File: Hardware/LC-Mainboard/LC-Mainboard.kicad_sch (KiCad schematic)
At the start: 1 part

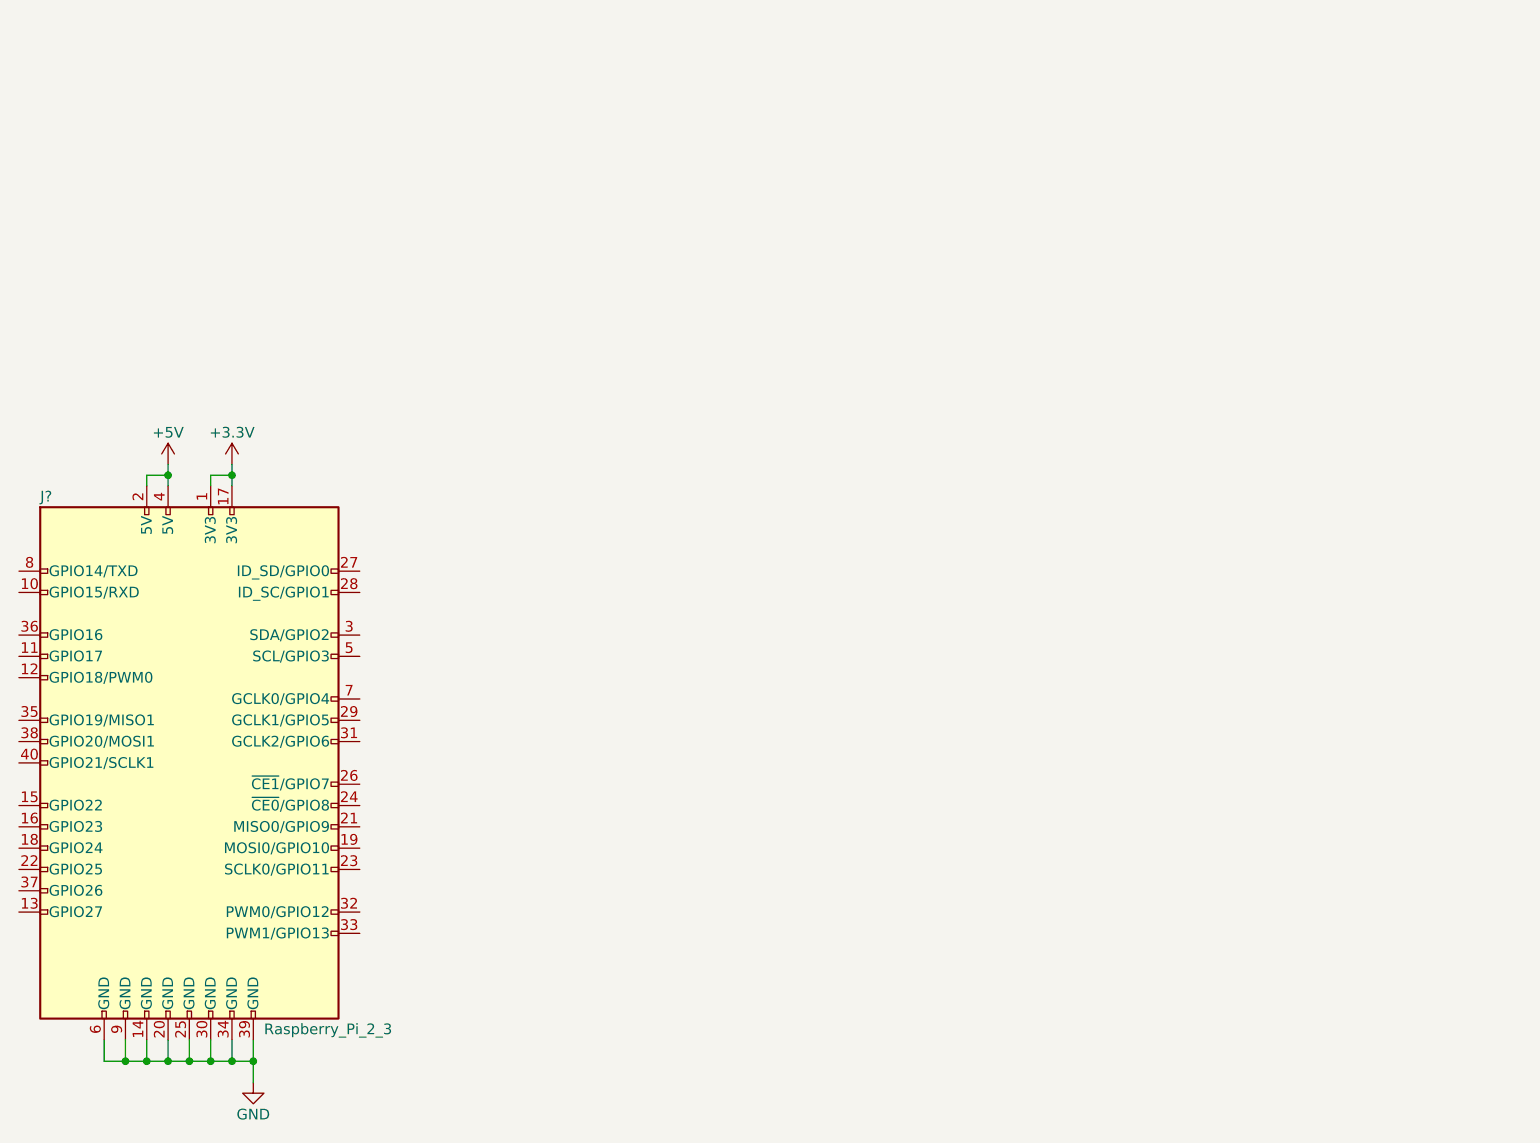
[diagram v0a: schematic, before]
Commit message: Add lib depend, remove bak and boilerplate
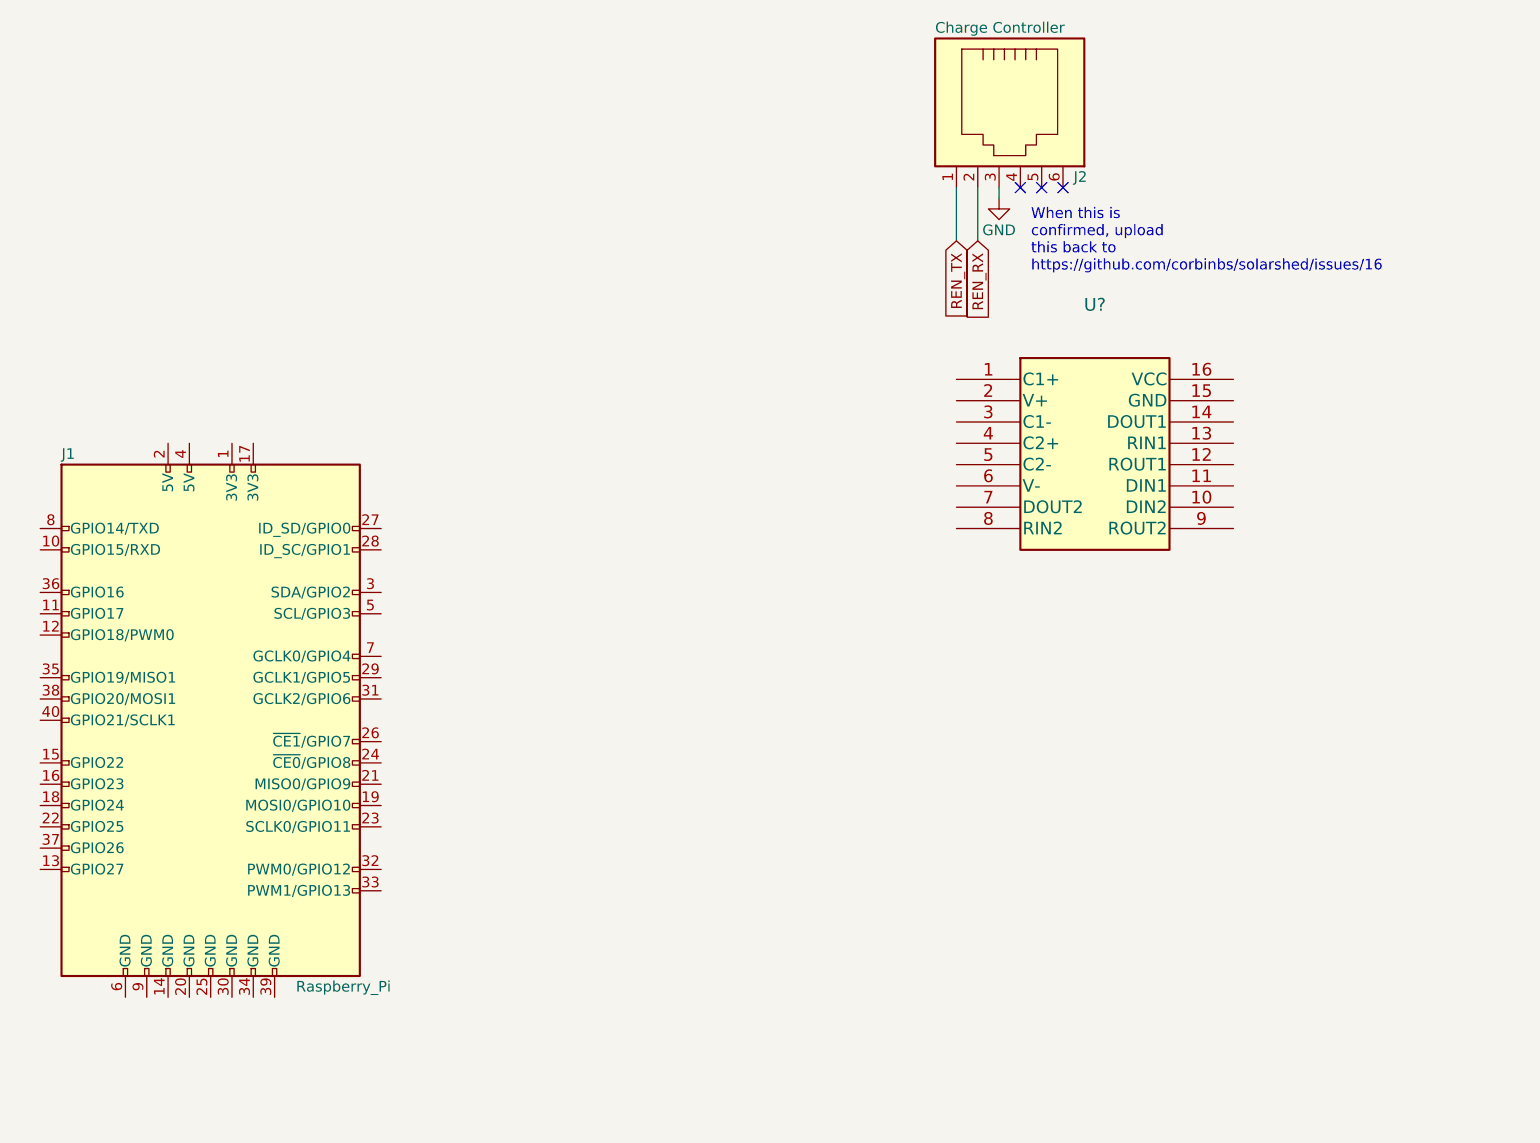
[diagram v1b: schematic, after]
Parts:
- removed J?: Raspberry_Pi_2_3, symbol Connector:Raspberry_Pi_2_3
- added J1: Raspberry_Pi, Connector_PinSocket_2.54mm:PinSocket_2x20_P2.54mm_Vertical, symbol Connector:Raspberry_Pi_2_3
- added J2: Charge Controller, Connector_RJ:RJ12_Amphenol_54601, symbol Connector:RJ12
- added U?: (no value), symbol KenwoodFox:MAX3232IDW
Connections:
- net GND: now also J2.3
- new net REN_RX: J2.2
- new net REN_TX: J2.1
- no-connect marks 0 -> 3
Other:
- note added: "When this is confirmed, upload this back to https://github.com/corbinbs/solarshed/issues/16"

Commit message: Update all
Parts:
- U?: value (none) -> MAX3232IDW; footprint (none) -> KenwoodFox:MAX3232IDW
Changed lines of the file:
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@@
       (effects (font (size 1.524 1.524)))
     )
-    (property "Value" "" (id 1) (at 251.46 52.07 0)
+    (property "Value" "MAX3232IDW" (id 1) (at 251.46 52.07 0)
       (effects (font (size 1.524 1.524)))
     )
-    (property "Footprint" "" (id 2) (at 251.46 66.04 0)
+    (property "Footprint" "KenwoodFox:MAX3232IDW" (id 2) (at 251.46 66.04 0)
       (effects (font (size 1.524 1.524)) hide)
     )

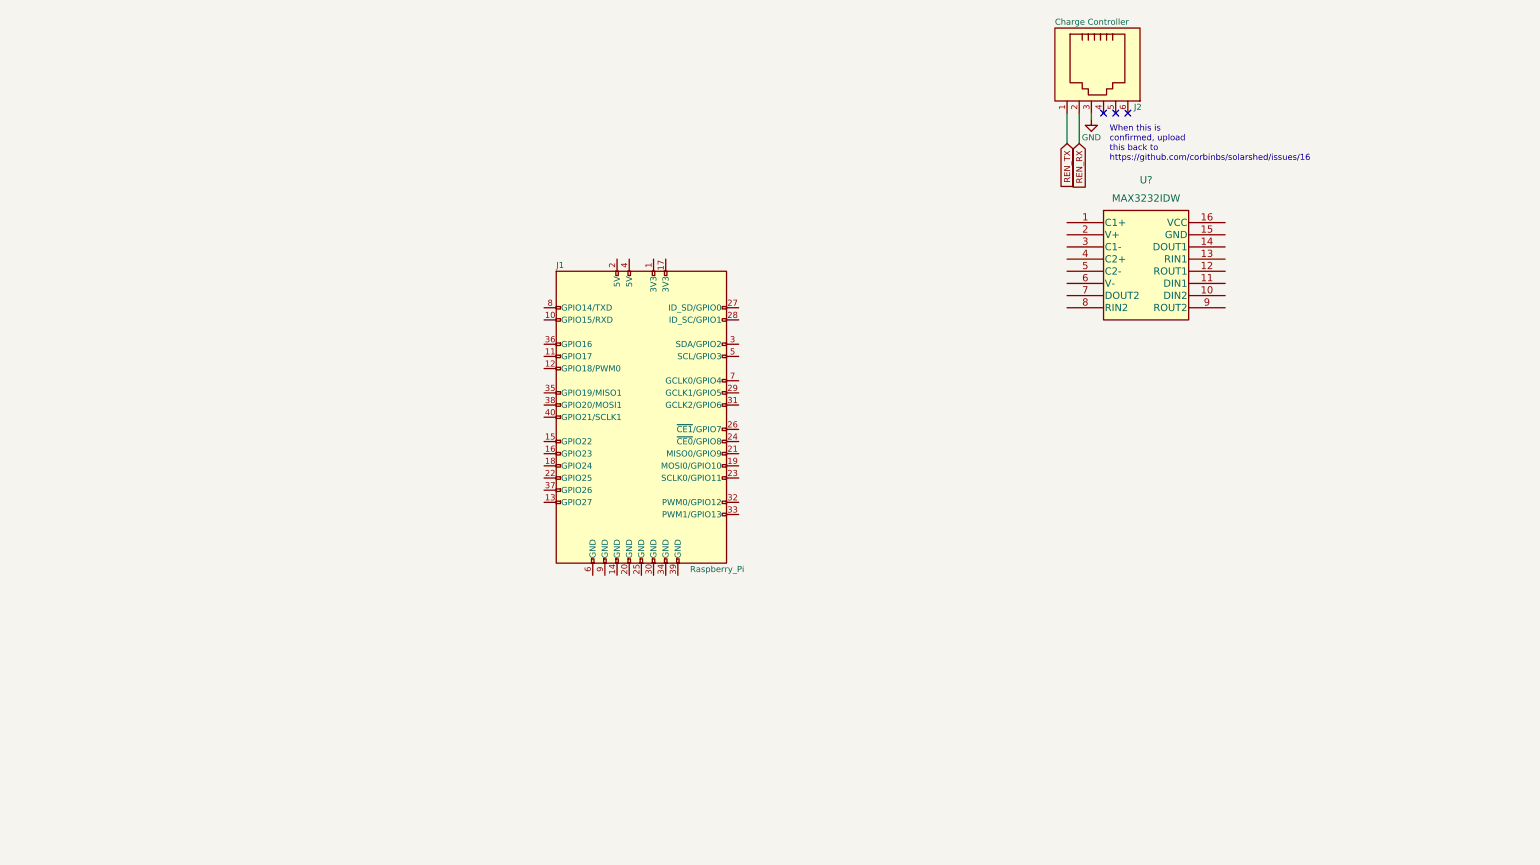
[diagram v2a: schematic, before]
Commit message: Fix encoder spacer, bump lib and implement max3232 in sch
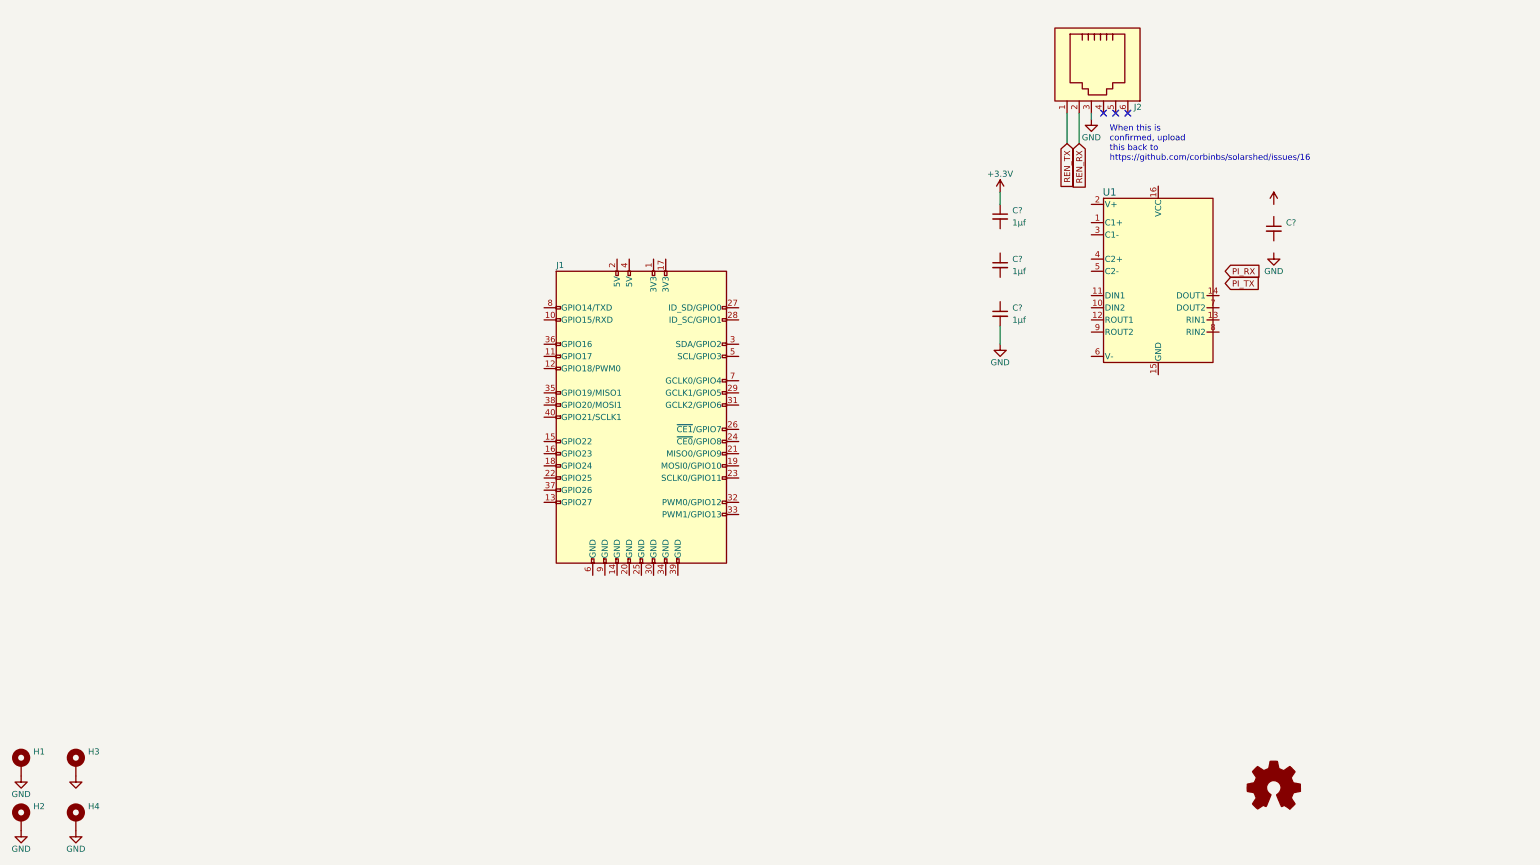
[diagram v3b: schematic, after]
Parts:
- added C? (x3): 1μf, symbol Device:C_Small
- added C?: (no value), symbol Device:C_Small
- added H1, H2, H3, H4: (no value), symbol Mechanical:MountingHole_Pad
- J1: value Raspberry_Pi -> (none); footprint Connector_PinSocket_2.54mm:PinSocket_2x20_P2.54mm_Vertical -> (none)
- J2: value Charge Controller -> (none); footprint Connector_RJ:RJ12_Amphenol_54601 -> (none)
- U1: renamed from U?; value MAX3232IDW -> (none)
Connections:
- net GND: now also C?.2, H1.1, H2.1, H3.1, H4.1
- new net +3V3: C?.1
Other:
- moved on the sheet: U1

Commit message: Bump
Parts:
- removed C? (x2): 1μf, symbol Device:C_Small
- removed C?: (no value), symbol Device:C_Small
- added C1, C3, C4: (no value), symbol Device:C_Small
- added D1, D2: (no value), symbol Device:LED
- added R1, R2: (no value), symbol Device:R_Small
- C2: renamed from C?; value 1μf -> (none)
- U1: footprint KenwoodFox:MAX3232IDW -> (none)
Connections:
- net +3V3: now also J1.1 (3V3), J1.17 (3V3), U1.16 (VCC), C1.1, R1.1, R2.1
- net GND: now also J1.14 (GND), J1.20 (GND), J1.25 (GND), J1.30 (GND), J1.34 (GND), J1.39 (GND), J1.6 (GND), J1.9 (GND), U1.15 (GND), C4.2
- net PI_RX: now also J1.10 (GPIO15/RXD), U1.12 (ROUT1), D1.1 (K)
- net PI_TX: now also J1.8 (GPIO14/TXD), U1.11 (DIN1), D2.1 (K)
- net REN_RX: now also U1.14 (DOUT1)
- net REN_TX: now also U1.13 (RIN1)
- net at U1.1 (C1+): now also C2.1
- net at U1.2 (V+): now also C1.2
- net at U1.3 (C1-): now also C2.2
- net at U1.4 (C2+): now also C3.1
- net at U1.5 (C2-): now also C3.2
- net at U1.6 (V-): now also C4.1
- net +5V: now reaches J1.2 (5V)
- net +5V: now also J1.4 (5V)
- new net: D2.2 (A), R2.2
- new net: D1.2 (A), R1.2
- no-connect marks 3 -> 7
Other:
- note added: "When this is confirmed, report back to https://github.com/corbinbs/solarshed/issues/16"
- note removed: "When this is confirmed, upload this back to https://github.com/corbinbs/solarshed/issues/16"
- moved on the sheet: C2, J2, U1

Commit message: Bump logo
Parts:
- C1, C2, C3, C4: value (none) -> 0.1μf; footprint (none) -> Capacitor_SMD:C_0805_2012Metric
- D1: value (none) -> SLR_RX; footprint (none) -> LED_SMD:LED_0805_2012Metric
- D2: value (none) -> SLR_TX; footprint (none) -> LED_SMD:LED_0805_2012Metric
- H1, H2, H3, H4: value (none) -> M_Hole; footprint (none) -> MountingHole:MountingHole_3mm_Pad
- J1: value (none) -> Raspberry_Pi; footprint (none) -> Connector_PinSocket_2.54mm:PinSocket_2x20_P2.54mm_Vertical
- J2: value (none) -> Charge Controller; footprint (none) -> Connector_RJ:RJ12_Amphenol_54601
- R1, R2: value (none) -> 100k; footprint (none) -> Resistor_SMD:R_0805_2012Metric
- U1: value (none) -> MAX3232IDW; footprint (none) -> KenwoodFox:MAX3232IDW
